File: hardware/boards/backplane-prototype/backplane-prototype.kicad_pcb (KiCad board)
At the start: 4 copper layers, 151.8 x 30.8 mm, 91 parts, among them J1 SLOT_1, J10 TC2030-IDC-NL SWD, J11 12V 3-WIRE FAN, J12 DS18B20 EXT SUPPLY, J2 XY308-2.54-3P / EXTERNAL CAN, J3 SLOT_2, J4 SLOT_3, J5 DC INPUT (GND / +VIN), J6 SLOT_4, J7 SLOT_5, J8 SLOT_6, J9 12V 3-WIRE FAN, Q1 AO3407A, Q2 2N7002, Q3 AO3407A, Q4 2N7002, U1 STM32C092GCU6, U2 LM5164DDAR, U3 LM5164DDAR, U4 INA237AIDGSR, U5 TCAN3413DR

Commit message: checkpoint: save backplane zone updates
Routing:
- net VIN_BUS: track 14.5 -> 0.00 mm
- net +3V3: track 221.8 -> 207.4 mm
- net GND: track 18.5 -> 12.2 mm
- net /Power Input, Monitor and Regulators/RON_3V3: track 1.94 -> 0.00 mm
- net /Power Input, Monitor and Regulators/RIPPLE_3V3: track 3.09 -> 1.50 mm
- net /Power Input, Monitor and Regulators/FB_3V3: track 8.18 -> 7.34 mm

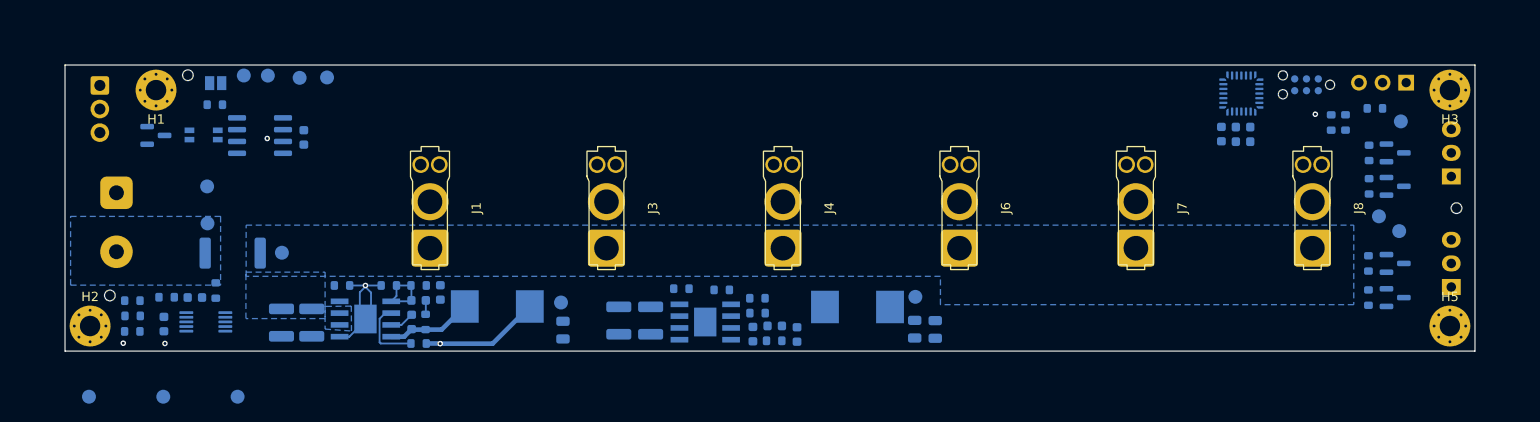
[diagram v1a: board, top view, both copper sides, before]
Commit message: hardware: consolidate backplane power and ground zones
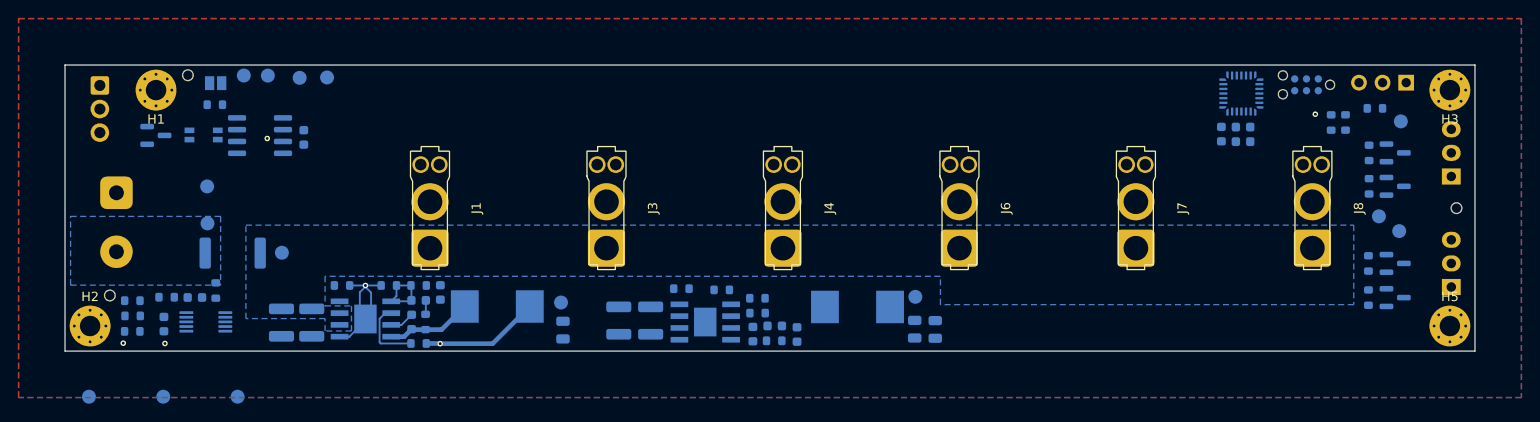
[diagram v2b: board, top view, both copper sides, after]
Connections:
- U1 pad 8: PGOOD_3V3 -> (no net)
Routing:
- added copper zone on B.Cu, net GND
- added copper zone on F.Cu, net GND
- added copper zone on In1.Cu, net GND
- added copper zone on In2.Cu, net GND
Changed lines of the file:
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@@
 			(size 0.136863 0.136863)
 			(layers "B.Cu" "B.Mask" "B.Paste")
-			(net "PGOOD_3V3")
 			(pinfunction "PA2_8")
 			(pintype "bidirectional")
@@
 	)
 	(zone
-		(net "VIN_BUS")
-		(layer "B.Cu")
-		(name "VIN_BUS_1")
+		(net "GND")
+		(layers "F.Cu" "B.Cu" "In1.Cu" "In2.Cu")
+		(name "GND_ALL_LAYERS")
 		(hatch edge 0.5)
-		(priority 2)
-		(connect_pads yes
+		(connect_pads
 			(clearance 0.5)
 		)
@@
 			(thermal_gap 0.5)
 			(thermal_bridge_width 0.5)
-			(smoothing fillet)
-			(radius 1)
-			(island_removal_mode 1)
+			(island_removal_mode 0)
 		)
 		(polygon
 			(pts
-				(xy 48.98 69) (xy 57.5 69) (xy 57.5 74) (xy 48.98 74)
+				(xy 24.5 41.7) (xy 186.3 41.7) (xy 186.3 82.5) (xy 24.5 82.5)
 			)
 		)
@@
 		(polygon
 			(pts
-				(xy 49 63.94) (xy 168.25 63.94) (xy 168.25 72.5) (xy 123.75 72.5) (xy 123.75 69.45) (xy 49 69.45)
+				(xy 48.98 63.94) (xy 168.25 63.94) (xy 168.25 72.5) (xy 123.75 72.5) (xy 123.75 69.45) (xy 57.5 69.45)
+				(xy 57.5 72.64) (xy 60.34 72.64) (xy 60.34 75.34) (xy 57.5 75.34) (xy 57.5 74) (xy 48.98 74)
 			)
 		)
@@
 		(name "VIN_RAW")
 		(hatch edge 0.5)
-		(connect_pads
-			(clearance 0.5)
-		)
-		(min_thickness 0.25)
-		(fill yes
-			(thermal_gap 0.5)
-			(thermal_bridge_width 0.5)
-			(island_removal_mode 1)
-		)
-		(polygon
-			(pts
-				(xy 30.1 63) (xy 46.25 63) (xy 46.25 70.4) (xy 30.1 70.4)
-			)
-		)
-	)
-	(zone
-		(net "VIN_BUS")
-		(layer "B.Cu")
-		(name "VIN_BUS_2")
-		(hatch edge 0.5)
-		(priority 3)
+		(priority 1)
 		(connect_pads yes
 			(clearance 0.5)
@@
 		(polygon
 			(pts
-				(xy 60.3 72.66) (xy 57.5 72.69) (xy 57.5 75.13) (xy 60.34 75.34) (xy 60.32 72.64)
+				(xy 30.1 63) (xy 46.25 63) (xy 46.25 70.4) (xy 30.1 70.4)
 			)
 		)

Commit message: checkpoint: save backplane layout updates
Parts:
- moved H8 10.4 mm to (27.8, 63.5)
- moved R12 8.46 mm to (48.9, 71.6), turned to 180 degrees
- moved C16 7.91 mm to (48.0, 74.3), turned to -90 degrees
- moved C15 4.22 mm to (47.3, 69.9), turned to 0 degrees
- moved R15 1.68 mm to (38.4, 75.6)
- moved R14 1.67 mm to (38.4, 72.3)
- moved R13 1.64 mm to (38.4, 74.0)
- moved R11 1.16 mm to (44.6, 70.8)
- moved U4 0.74 mm to (44.0, 74.6), turned to 0 degrees
- moved TP5 0.69 mm to (44.8, 60.5)
- moved C4 0.65 mm to (82.5, 75.2)
- moved TP3 0.49 mm to (82.5, 72.0)
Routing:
- net /CAN-FD and Six Slots/CAN_BUS_N: track 0.00 -> 100.1 mm
- net /CAN-FD and Six Slots/CAN_BUS_P: track 0.00 -> 100.0 mm
- net +3V3: track 207.4 -> 227.9 mm
- net /Power Input, Monitor and Regulators/INA_IN_N: track 0.00 -> 9.64 mm
- net /Power Input, Monitor and Regulators/INA_IN_P: track 0.00 -> 8.91 mm
- net VIN_BUS: track 0.00 -> 8.08 mm
- net I2C_SCL: track 0.00 -> 3.13 mm, vias 0 -> 1
- net I2C_SDA: track 0.00 -> 3.08 mm, vias 0 -> 1
- net INA_ALERT: track 0.00 -> 3.07 mm, vias 0 -> 1
- net GND: track 12.2 -> 14.6 mm, vias 1 -> 11
- net /Power Input, Monitor and Regulators/RIPPLE_3V3: track 1.50 -> 3.10 mm

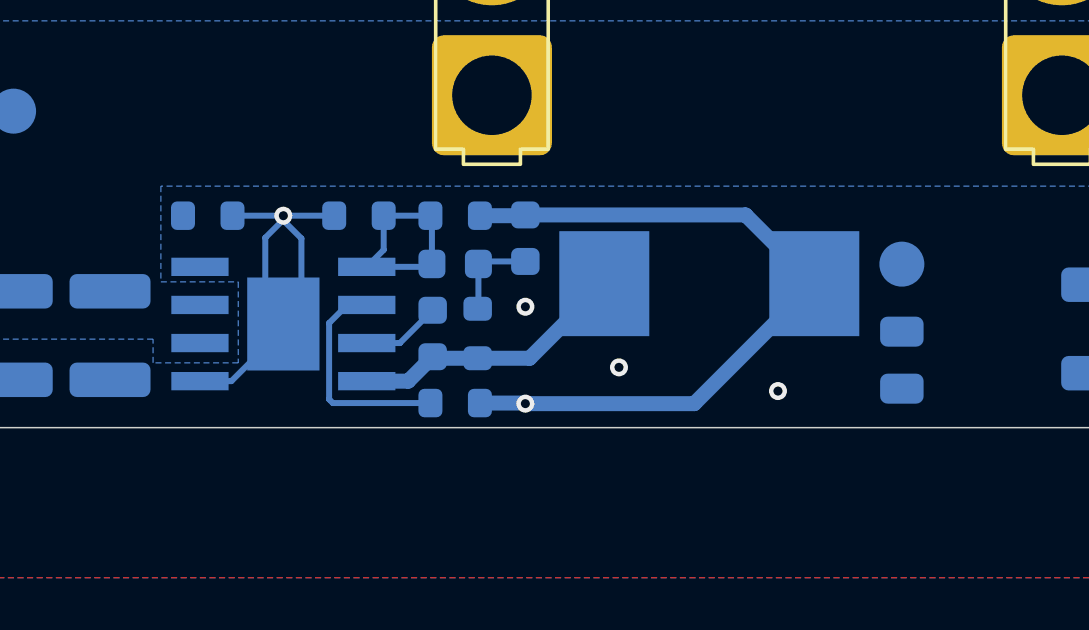
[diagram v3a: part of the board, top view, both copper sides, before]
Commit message: hardware: remove unused 3v3 power-good pull-up
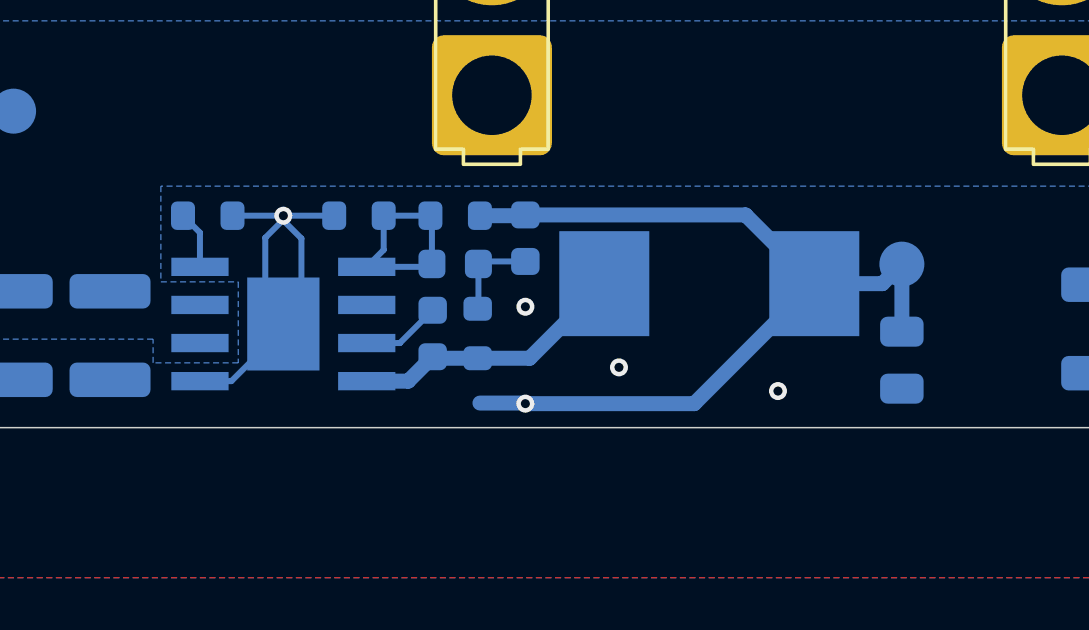
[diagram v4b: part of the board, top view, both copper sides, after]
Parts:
- removed R5: 10k, Resistor_SMD:R_0603_1608Metric
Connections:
- U2 pad 6: PGOOD_3V3 -> (no net)
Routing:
- net PGOOD_3V3: track 7.47 -> 0.00 mm
- net +3V3: track 227.9 -> 233.3 mm
- net /Power Input, Monitor and Regulators/RON_3V3: track 0.00 -> 1.94 mm
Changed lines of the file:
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@@
 			(size 1.91 0.61)
 			(layers "B.Cu" "B.Mask" "B.Paste")
-			(net "PGOOD_3V3")
 			(pinfunction "PGOOD_6")
 			(pintype "open_collector")
@@
 	(footprint "Resistor_SMD:R_0603_1608Metric"
 		(layer "B.Cu")
-		(at 67.57 76.68 180)
-		(descr "Resistor SMD 0603 (1608 Metric), square (rectangular) end terminal, IPC-7351 nominal, (Body size source: IPC-SM-782 page 72, https://www.pcb-3d.com/wordpress/wp-content/uploads/ipc-sm-782a_amendment_1_and_2.pdf)")
-		(tags "resistor")
-		(property "Reference" "R5"
-			(at 0 1.43 0)
-			(layer "B.SilkS")
-			(effects
-				(font
-					(size 1 1)
-					(thickness 0.15)
-				)
-				(justify mirror)
-			)
-		)
-		(property "Value" "10k"
-			(at 0 -1.43 0)
-			(layer "B.Fab")
-			(effects
-				(font
-					(size 1 1)
-					(thickness 0.15)
-				)
-				(justify mirror)
-			)
-		)
-		(property "Datasheet" ""
-			(at 0 0 0)
-			(layer "B.Fab")
-			(hide yes)
-			(effects
-				(font
-					(size 1.27 1.27)
-				)
-				(justify mirror)
-			)
-		)
-		(property "Description" ""
-			(at 0 0 0)
-			(layer "B.Fab")
-			(hide yes)
-			(effects
-				(font
-					(size 1.27 1.27)
-				)
-				(justify mirror)
-			)
-		)
-		(property "KiLib_Generator" "SMD_2terminal_chip_molded"
-			(at 0 0 0)
-			(layer "B.SilkS")
-			(hide yes)
-			(effects
-				(font
-					(size 1 1)
-					(thickness 0.15)
-				)
-				(justify mirror)
-			)
-		)
-		(property "MPN" "0603WAF1002T5E"
-			(at 0 0 0)
-			(unlocked yes)
-			(layer "B.Fab")
-			(hide yes)
-			(effects
-				(font
-					(size 1 1)
-					(thickness 0.15)
-				)
-				(justify mirror)
-			)
-		)
-		(property "Manufacturer" "UNI-ROYAL (Uniroyal Elec)"
-			(at 0 0 0)
-			(unlocked yes)
-			(layer "B.Fab")
-			(hide yes)
-			(effects
-				(font
-					(size 1 1)
-					(thickness 0.15)
-				)
-				(justify mirror)
-			)
-		)
-		(property "LCSC" "C25804"
-			(at 0 0 0)
-			(unlocked yes)
-			(layer "B.Fab")
-			(hide yes)
-			(effects
-				(font
-					(size 1 1)
-					(thickness 0.15)
-				)
-				(justify mirror)
-			)
-		)
-		(property "Tolerance" "1%"
-			(at 0 0 0)
-			(unlocked yes)
-			(layer "B.Fab")
-			(hide yes)
-			(effects
-				(font
-					(size 1 1)
-					(thickness 0.15)
-				)
-				(justify mirror)
-			)
-		)
-		(property ki_fp_filters "R_*")
-		(sheetname "/Power Input, Monitor and Regulators/")
-		(sheetfile "01_power_input.kicad_sch")
-		(units
-			(unit
-				(name "A")
-				(pins "1" "2")
-			)
-		)
-		(attr smd)
-		(duplicate_pad_numbers_are_jumpers no)
-		(fp_line
-			(start -0.237258 0.5225)
-			(end 0.237258 0.5225)
-			(stroke
-				(width 0.12)
-				(type solid)
-			)
-			(layer "B.SilkS")
-		)
-		(fp_line
-			(start -0.237258 -0.5225)
-			(end 0.237258 -0.5225)
-			(stroke
-				(width 0.12)
-				(type solid)
-			)
-			(layer "B.SilkS")
-		)
-		(fp_rect
-			(start -1.48 0.73)
-			(end 1.48 -0.73)
-			(stroke
-				(width 0.05)
-				(type solid)
-			)
-			(fill no)
-			(layer "B.CrtYd")
-		)
-		(fp_rect
-			(start -0.8 0.4125)
-			(end 0.8 -0.4125)
-			(stroke
-				(width 0.1)
-				(type solid)
-			)
-			(fill no)
-			(layer "B.Fab")
-		)
-		(fp_text user "${REFERENCE}"
-			(at 0 0 0)
-			(layer "B.Fab")
-			(effects
-				(font
-					(size 0.4 0.4)
-					(thickness 0.06)
-				)
-				(justify mirror)
-			)
-		)
-		(pad "1" smd roundrect
-			(at -0.825 0 180)
-			(size 0.8 0.95)
-			(layers "B.Cu" "B.Mask" "B.Paste")
-			(roundrect_rratio 0.25)
-			(net "+3V3")
-			(pintype "passive")
-		)
-		(pad "2" smd roundrect
-			(at 0.825 0 180)
-			(size 0.8 0.95)
-			(layers "B.Cu" "B.Mask" "B.Paste")
-			(roundrect_rratio 0.25)
-			(net "PGOOD_3V3")
-			(pintype "passive")
-		)
-		(embedded_fonts no)
-		(model "${KICAD10_3DMODEL_DIR}/Resistor_SMD.3dshapes/R_0603_1608Metric.step"
-			(offset
-				(xyz 0 0 0)
-			)
-			(scale
-				(xyz 1 1 1)
-			)
-			(rotate
-				(xyz 0 0 0)
-			)
-		)
-	)
-	(footprint "Resistor_SMD:R_0603_1608Metric"
-		(layer "B.Cu")
 		(at 165.82 52.89 -90)
 		(descr "Resistor SMD 0603 (1608 Metric), square (rectangular) end terminal, IPC-7351 nominal, (Body size source: IPC-SM-782 page 72, https://www.pcb-3d.com/wordpress/wp-content/uploads/ipc-sm-782a_amendment_1_and_2.pdf)")
@@
 	)
 	(segment
+		(start 79.54 72.7)
+		(end 81.81 72.7)
+		(width 0.5)
+		(layer "B.Cu")
+		(net "+3V3")
+	)
+	(segment
+		(start 81.81 72.7)
+		(end 82.46 72.05)
+		(width 0.5)
+		(layer "B.Cu")
+		(net "+3V3")
+	)
+	(segment
+		(start 82.46 72.05)
+		(end 82.46 74.3)
+		(width 0.5)
+		(layer "B.Cu")
+		(net "+3V3")
+	)
+	(segment
 		(start 37.575 72.34)
 		(end 37.575 76.68)
@@
 	)
 	(segment
+		(start 58.4975 70.435)
+		(end 59.0625 71)
+		(width 0.2)
+		(layer "B.Cu")
+		(net "/Power Input, Monitor and Regulators/RON_3V3")
+	)
+	(segment
+		(start 59.0625 71)
+		(end 59.0625 72.14)
+		(width 0.2)
+		(layer "B.Cu")
+		(net "/Power Input, Monitor and Regulators/RON_3V3")
+	)
+	(segment
 		(start 64.6225 72.14)
 		(end 66.698333 72.14)
@@
 	)
 	(segment
-		(start 63.4925 76.68)
-		(end 63.3675 76.555)
-		(width 0.2)
-		(layer "B.Cu")
-		(net "PGOOD_3V3")
-	)
-	(segment
-		(start 63.3675 74.015)
-		(end 63.9725 73.41)
-		(width 0.2)
-		(layer "B.Cu")
-		(net "PGOOD_3V3")
-	)
-	(segment
-		(start 63.9725 73.41)
-		(end 64.6225 73.41)
-		(width 0.2)
-		(layer "B.Cu")
-		(net "PGOOD_3V3")
-	)
-	(segment
-		(start 63.3675 76.555)
-		(end 63.3675 74.015)
-		(width 0.2)
-		(layer "B.Cu")
-		(net "PGOOD_3V3")
-	)
-	(segment
-		(start 66.745 76.68)
-		(end 63.4925 76.68)
-		(width 0.2)
-		(layer "B.Cu")
-		(net "PGOOD_3V3")
-	)
-	(segment

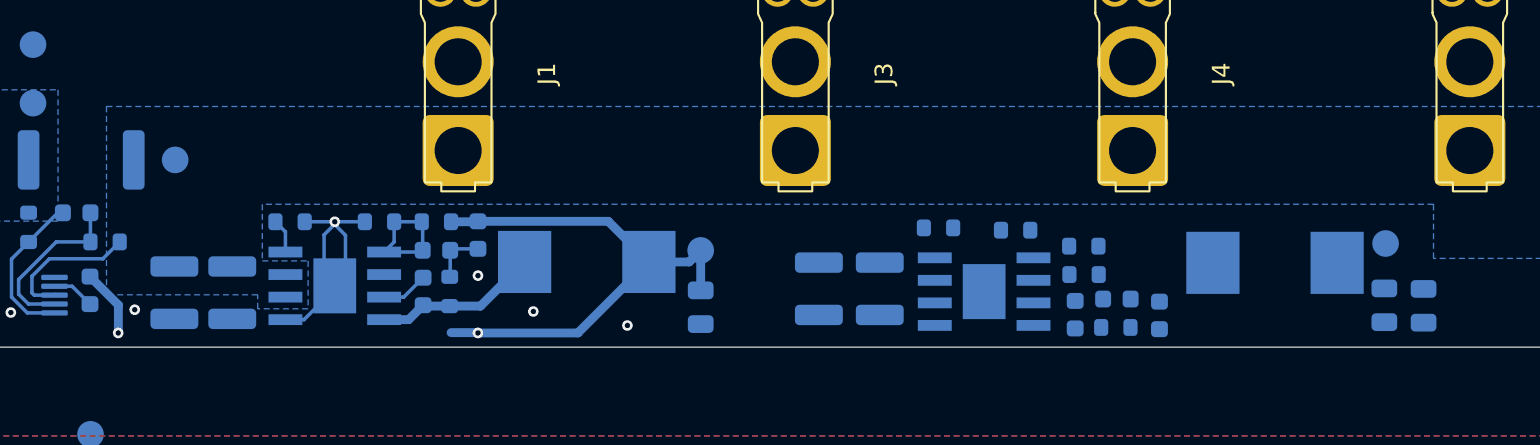
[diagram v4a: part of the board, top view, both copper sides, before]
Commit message: checkpoint: save 3v3 buck layout updates
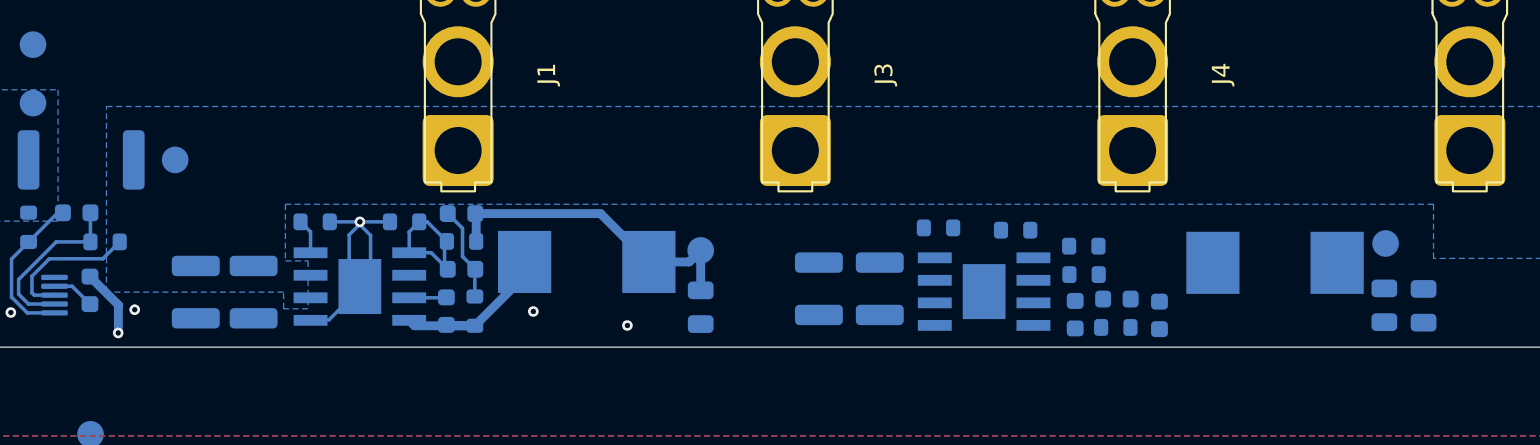
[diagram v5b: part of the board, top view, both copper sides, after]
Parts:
- moved R2 1.80 mm to (69.0, 71.5)
- moved R4 1.80 mm to (69.7, 75.5)
- moved C6 1.77 mm to (69.0, 73.1)
- moved C3 1.72 mm to (68.1, 75.5)
- moved C5 1.52 mm to (69.0, 70.0), turned to 0 degrees
- moved U2 1.42 mm to (63.3, 74.1)
- moved R3 1.42 mm to (65.8, 70.4)
- moved R1 1.42 mm to (60.7, 70.4)
- moved C2 1.21 mm to (57.3, 74.4)
- moved C1 1.21 mm to (54.0, 74.4)
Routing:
- net +3V3: track 233.3 -> 220.9 mm, vias 5 -> 4
- net /Power Input, Monitor and Regulators/RIPPLE_3V3: track 3.10 -> 5.32 mm
- net /Power Input, Monitor and Regulators/FB_3V3: track 7.34 -> 8.25 mm
- net /Power Input, Monitor and Regulators/SW_3V3: track 9.47 -> 10.4 mm
- net /Power Input, Monitor and Regulators/BST_3V3: track 2.65 -> 2.10 mm
- net GND: vias 11 -> 10

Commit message: checkpoint: save backplane power layout progress
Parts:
- moved R10 7.43 mm to (103.3, 80.8)
- moved C1 0.20 mm to (54.2, 74.4)
- moved C2 0.20 mm to (57.5, 74.4)
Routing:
- net +3V3: track 220.9 -> 227.0 mm, vias 4 -> 5
- net VIN_BUS: track 8.08 -> 11.9 mm, vias 0 -> 7
- net GND: vias 10 -> 15
- added copper zone on F.Cu, net VIN_BUS
- added copper zone on In1.Cu, net VIN_BUS
- added copper zone on In2.Cu, net VIN_BUS
